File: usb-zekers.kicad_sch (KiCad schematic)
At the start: 0 parts

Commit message: Wire more stuff
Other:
- added sheet Power (power.kicad_sch)
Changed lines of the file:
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@@
+    )
+  )
+  (sheet (at 168.275 111.76) (size 12.7 3.81) (fields_autoplaced)
+    (stroke (width 0.1524) (type solid))
+    (fill (color 0 0 0 0.0000))
+    (property "Sheetname" "Power" (at 168.275 111.0484 0)
+      (effects (font (size 1.27 1.27)) (justify left bottom))
+    )
+    (property "Sheetfile" "power.kicad_sch" (at 168.275 116.1546 0)
+      (effects (font (size 1.27 1.27)) (justify left top))
+    )
+    (instances
+      (project "usb-zekers"
+        (path "/1eef11ed-4055-4fe6-b7fc-0d497914d6cc" (page "6"))
+      )
     )
   )

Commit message: Whole bunch of changes to all kinds of things
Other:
- sheet Connectors ports: added CC_PORT0{CC1, CC2}, SWD{SWDIO,SWDCLK}, VBUS_PORT0, VBUS_PORTA, ~{RESET}; removed none
- sheet MCU ports: added I2C{SDA,SCL}, LED_PORT0{R,G}, NCP0_CLIND, NCP0_EN, NCP0_INT, SWD{SWDIO,SWDCLK}, UCPD1{CC1,CC2}, ~{RESET}; removed none
- sheet Power conversion PORT0 ports: added I2C{SDA,SCL}, NCP0_CLIND, NCP0_EN, NCP0_INT, NCP0_VIN, NCP0_VOUT; removed none
- sheet User Interface ports: added LED_PORT0{R,G}, ~{RESET}; removed none

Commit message: WIP on vconn
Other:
- added sheet VCONN (vconn.kicad_sch)
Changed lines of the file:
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@@
-	(wire
-		(pts
-			(xy 137.16 121.92) (xy 181.61 121.92)
-		)
-		(stroke
-			(width 0)
-			(type default)
-		)
-	)
 	(wire
 		(pts
@@
 		(pts
 			(xy 85.09 93.98) (xy 85.09 106.68)
-		)
-		(stroke
-			(width 0)
-			(type default)
-		)
-	)
-	(wire
-		(pts
-			(xy 181.61 102.87) (xy 181.61 121.92)
 		)
 		(stroke
@@
 				)
 			)
+		)
+	)
+	(sheet
+		(at 161.29 120.65)
+		(size 35.56 24.13)
+		(fields_autoplaced yes)
+		(stroke
+			(width 0.1524)
+			(type solid)
+		)
+		(fill
+			(color 0 0 0 0.0000)
+		)
+		(property "Sheetname" "VCONN"
+			(at 161.29 119.9384 0)
+			(effects
+				(font
+					(size 1.27 1.27)
+				)
+				(justify left bottom)
+			)
+		)
+		(property "Sheetfile" "vconn.kicad_sch"
+			(at 161.29 145.3646 0)
+			(effects
+				(font
+					(size 1.27 1.27)
+				)
+				(justify left top)
+			)
+		)
+		(instances
+			(project "usb-zekers"
+				(path "/1eef11ed-4055-4fe6-b7fc-0d497914d6cc"
+					(page "7")
+				)
+			)

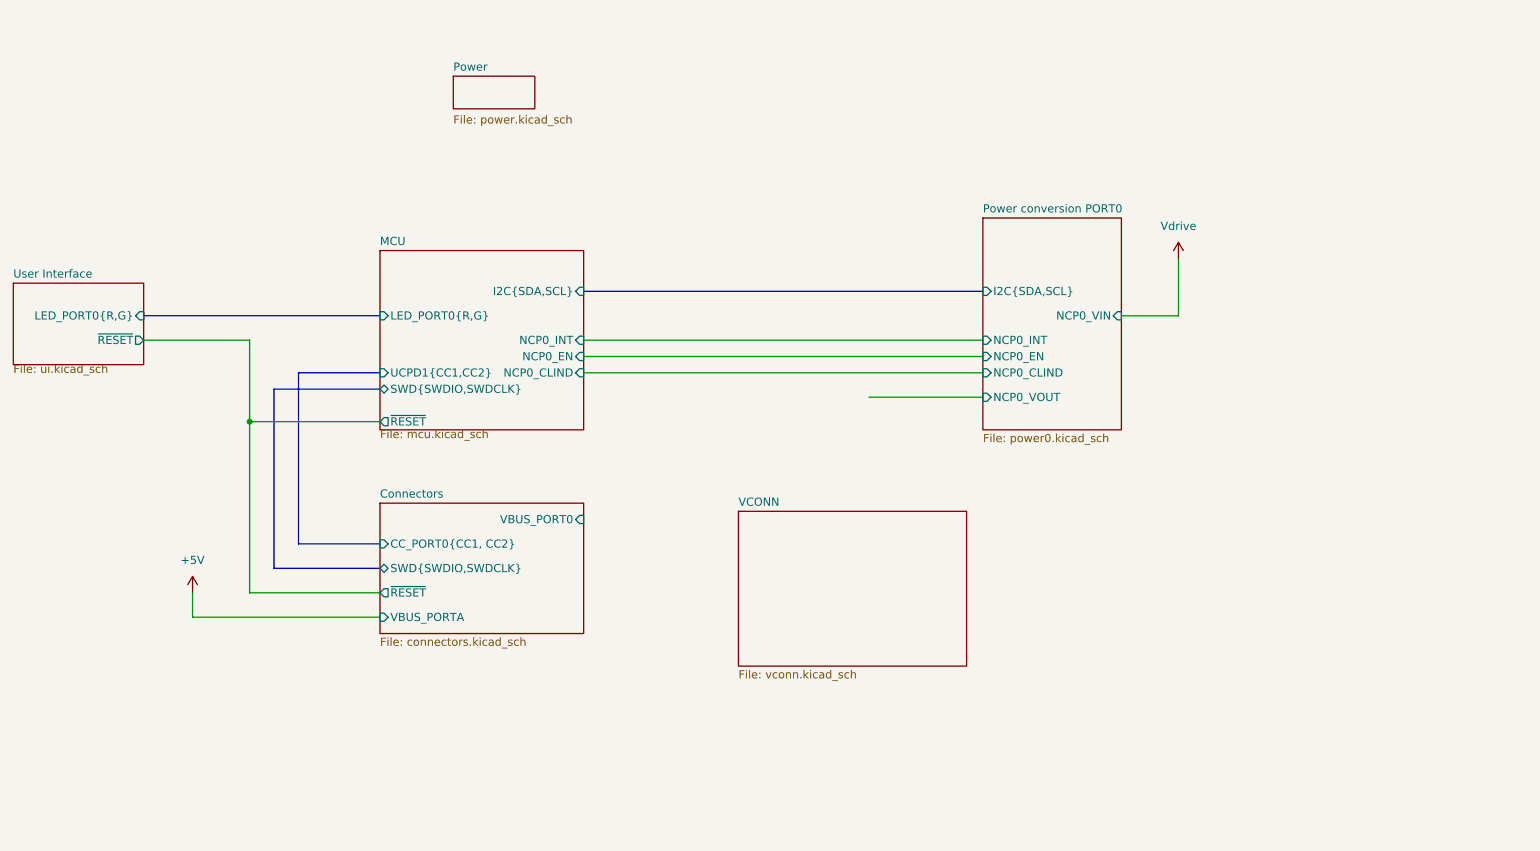
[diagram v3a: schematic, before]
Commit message: wire up vconn stuff
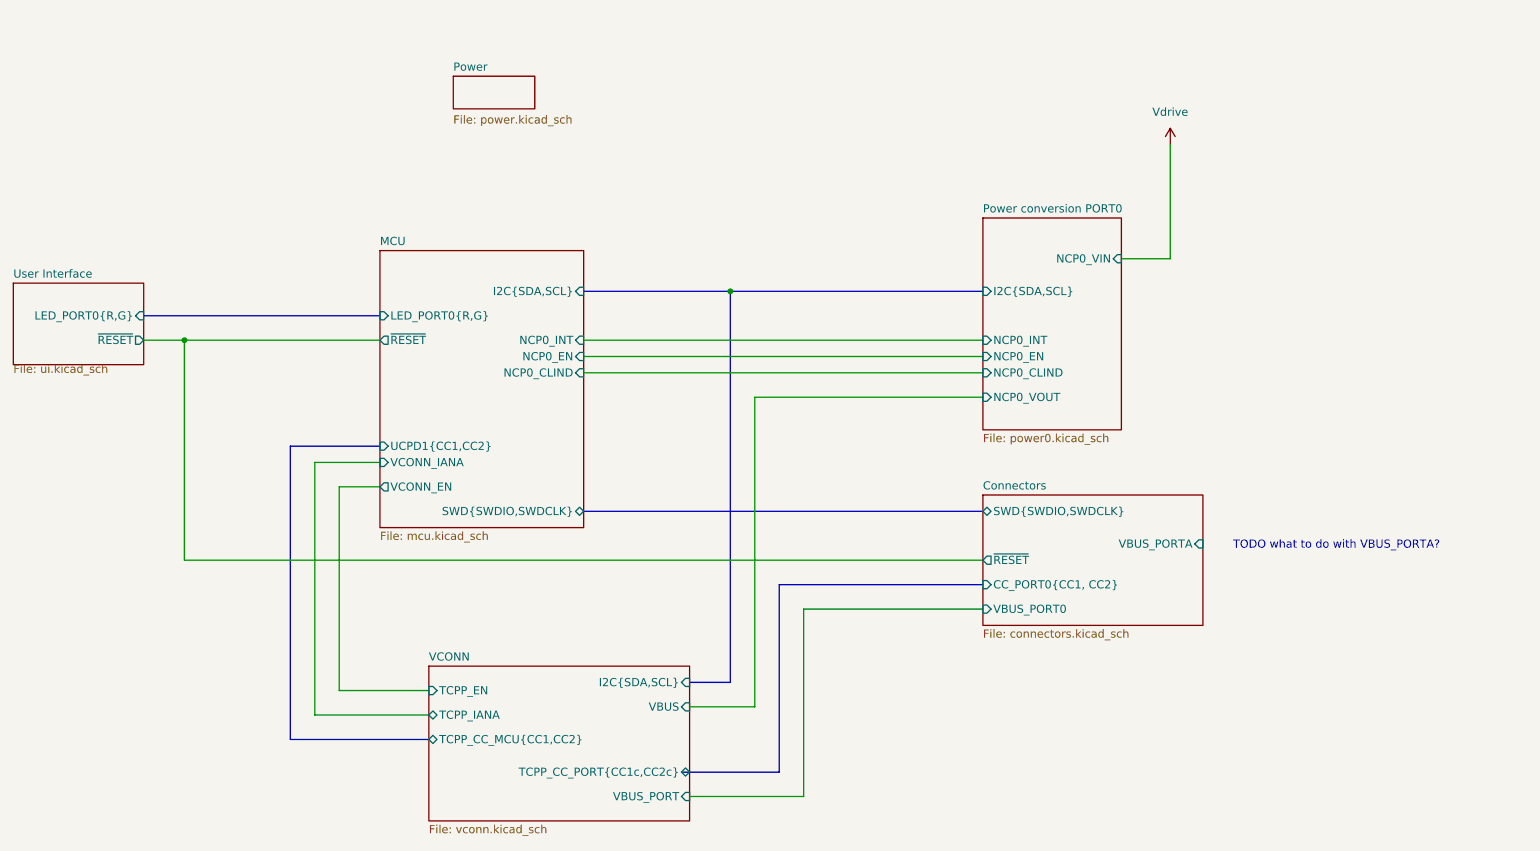
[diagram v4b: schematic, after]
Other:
- sheet MCU ports: added VCONN_EN, VCONN_IANA; removed none
- sheet VCONN ports: added I2C{SDA,SCL}, TCPP_CC_MCU{CC1,CC2}, TCPP_CC_PORT{CC1c,CC2c}, TCPP_EN, TCPP_IANA, VBUS, VBUS_PORT; removed none
- note added: "TODO what to do with VBUS_PORTA?"

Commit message: Wire up vconn and analog pins
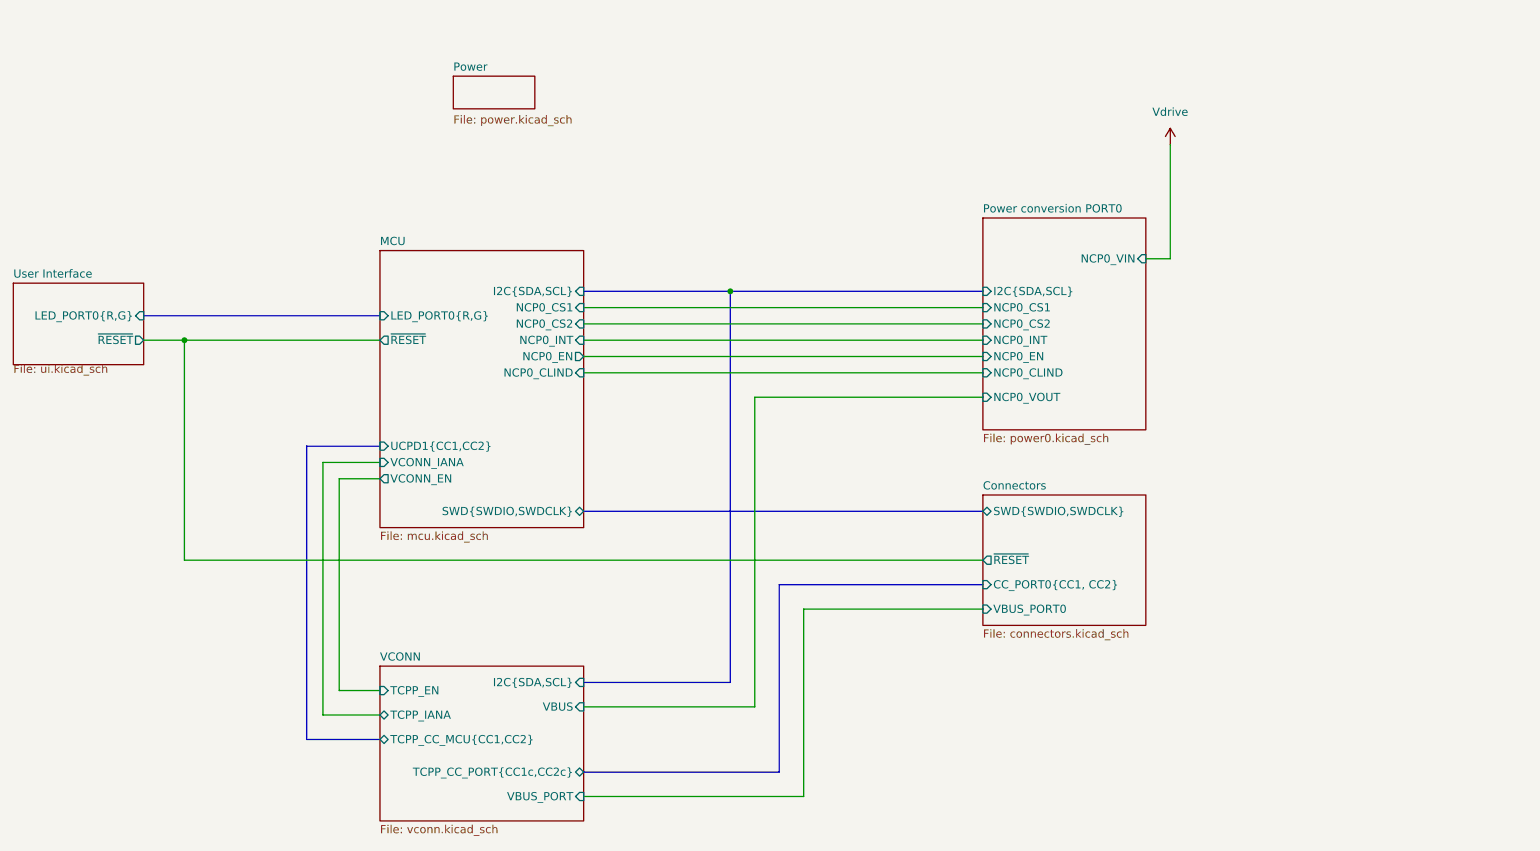
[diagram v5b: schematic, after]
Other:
- sheet Connectors ports: added none; removed VBUS_PORTA
- sheet MCU ports: added NCP0_CS1, NCP0_CS2; removed none
- sheet Power conversion PORT0 ports: added NCP0_CS1, NCP0_CS2; removed none
- note removed: "TODO what to do with VBUS_PORTA?"
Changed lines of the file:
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@@
 		(color 0 0 0 0)
 	)
-	(wire
-		(pts
-			(xy 228.6 81.28) (xy 220.98 81.28)
+	(bus
+		(pts
+			(xy 137.16 147.32) (xy 160.02 147.32)
 		)
 		(stroke
@@
 		)
 	)
-	(bus
-		(pts
-			(xy 153.67 147.32) (xy 160.02 147.32)
+	(wire
+		(pts
+			(xy 137.16 88.9) (xy 199.39 88.9)
 		)
 		(stroke
@@
 		)
 	)
+	(wire
+		(pts
+			(xy 224.79 81.28) (xy 228.6 81.28)
+		)
+		(stroke
+			(width 0)
+			(type default)
+		)
+	)
 	(bus
 		(pts
@@
 	(bus
 		(pts
-			(xy 91.44 110.49) (xy 91.44 156.21)
+			(xy 93.98 110.49) (xy 93.98 156.21)
+		)
+		(stroke
+			(width 0)
+			(type default)
+		)
+	)
+	(wire
+		(pts
+			(xy 137.16 165.1) (xy 171.45 165.1)
 		)
 		(stroke
@@
 	(bus
 		(pts
-			(xy 105.41 110.49) (xy 91.44 110.49)
+			(xy 105.41 110.49) (xy 93.98 110.49)
 		)
 		(stroke
@@
 	(wire
 		(pts
-			(xy 99.06 148.59) (xy 113.03 148.59)
-		)
-		(stroke
-			(width 0)
-			(type default)
-		)
-	)
-	(wire
-		(pts
-			(xy 105.41 116.84) (xy 99.06 116.84)
+			(xy 99.06 148.59) (xy 105.41 148.59)
+		)
+		(stroke
+			(width 0)
+			(type default)
+		)
+	)
+	(wire
+		(pts
+			(xy 105.41 115.57) (xy 99.06 115.57)
 		)
 		(stroke
@@
 	(wire
 		(pts
-			(xy 153.67 151.13) (xy 163.83 151.13)
-		)
-		(stroke
-			(width 0)
-			(type default)
-		)
-	)
-	(wire
-		(pts
-			(xy 153.67 165.1) (xy 171.45 165.1)
-		)
-		(stroke
-			(width 0)
-			(type default)
-		)
-	)
-	(wire
-		(pts
 			(xy 74.93 93.98) (xy 105.41 93.98)
 		)
@@
 	(wire
 		(pts
-			(xy 95.25 113.03) (xy 95.25 152.4)
+			(xy 96.52 113.03) (xy 96.52 152.4)
 		)
 		(stroke
@@
 		)
 	)
+	(bus
+		(pts
+			(xy 137.16 161.29) (xy 167.64 161.29)
+		)
+		(stroke
+			(width 0)
+			(type default)
+		)
+	)
 	(wire
 		(pts
@@
 	(wire
 		(pts
+			(xy 137.16 91.44) (xy 199.39 91.44)
+		)
+		(stroke
+			(width 0)
+			(type default)
+		)
+	)
+	(wire
+		(pts
 			(xy 74.93 128.27) (xy 74.93 93.98)
 		)
@@
 	(bus
 		(pts
-			(xy 91.44 156.21) (xy 113.03 156.21)
+			(xy 93.98 156.21) (xy 105.41 156.21)
+		)
+		(stroke
+			(width 0)
+			(type default)
+		)
+	)
+	(wire
+		(pts
+			(xy 137.16 151.13) (xy 163.83 151.13)
 		)
 		(stroke
@@
 	(wire
 		(pts
-			(xy 99.06 116.84) (xy 99.06 148.59)
+			(xy 99.06 115.57) (xy 99.06 148.59)
 		)
 		(stroke
@@
 	(wire
 		(pts
-			(xy 105.41 113.03) (xy 95.25 113.03)
-		)
-		(stroke
-			(width 0)
-			(type default)
-		)
-	)
-	(wire
-		(pts
-			(xy 95.25 152.4) (xy 113.03 152.4)
-		)
-		(stroke
-			(width 0)
-			(type default)
-		)
-	)
-	(bus
-		(pts
-			(xy 152.4 161.29) (xy 167.64 161.29)
-		)
-		(stroke
-			(width 0)
-			(type default)
-		)
-	)
-	(text "TODO what to do with VBUS_PORTA?\n"
-		(exclude_from_sim no)
-		(at 254.508 125.984 0)
-		(effects
-			(font
-				(size 1.27 1.27)
-			)
+			(xy 105.41 113.03) (xy 96.52 113.03)
+		)
+		(stroke
+			(width 0)
+			(type default)
+		)
+	)
+	(wire
+		(pts
+			(xy 96.52 152.4) (xy 105.41 152.4)
+		)
+		(stroke
+			(width 0)
+			(type default)
 		)
 	)
@@
 	(sheet
 		(at 199.39 118.11)
-		(size 34.29 20.32)
+		(size 25.4 20.32)
 		(fields_autoplaced yes)
 		(stroke
@@
 				)
 				(justify left)
-			)
-		)
-		(pin "VBUS_PORTA" input
-			(at 233.68 125.73 0)
-			(effects
-				(font
-					(size 1.27 1.27)
-				)
-				(justify right)
 			)
 		)
@@
 	)
 	(sheet
-		(at 113.03 144.78)
-		(size 40.64 24.13)
+		(at 105.41 144.78)
+		(size 31.75 24.13)
 		(fields_autoplaced yes)
 		(stroke
@@
 		)
 		(property "Sheetname" "VCONN"
-			(at 113.03 144.0684 0)
+			(at 105.41 144.0684 0)
 			(effects
 				(font
@@
 		)
 		(property "Sheetfile" "vconn.kicad_sch"
-			(at 113.03 169.4946 0)
+			(at 105.41 169.4946 0)
 			(effects
 				(font
@@
 		)
 		(pin "TCPP_EN" input
-			(at 113.03 148.59 180)
+			(at 105.41 148.59 180)
 			(effects
 				(font
@@
 		)
 		(pin "TCPP_CC_MCU{CC1,CC2}" bidirectional
-			(at 113.03 156.21 180)
+			(at 105.41 156.21 180)
 			(effects
 				(font
@@
 		)
 		(pin "TCPP_IANA" bidirectional
-			(at 113.03 152.4 180)
+			(at 105.41 152.4 180)
 			(effects
 				(font
@@
 		)
 		(pin "I2C{SDA,SCL}" input
-			(at 153.67 147.32 0)
+			(at 137.16 147.32 0)
 			(effects
 				(font
@@
 		)
 		(pin "VBUS" input
-			(at 153.67 151.13 0)
+			(at 137.16 151.13 0)
 			(effects
 				(font
@@
 		)
 		(pin "TCPP_CC_PORT{CC1c,CC2c}" bidirectional
-			(at 153.67 161.29 0)
+			(at 137.16 161.29 0)
 			(effects
 				(font
@@
 		)
 		(pin "VBUS_PORT" input
-			(at 153.67 165.1 0)
+			(at 137.16 165.1 0)
 			(effects
 				(font
@@
 			)
 		)
-		(pin "NCP0_EN" input
-			(at 137.16 96.52 0)
-			(effects
-				(font
-					(size 1.27 1.27)
-				)
-				(justify right)
-			)
-		)
 		(pin "NCP0_INT" input
 			(at 137.16 93.98 0)
@@
 		)
 		(pin "VCONN_EN" output
-			(at 105.41 116.84 180)
-			(effects
-				(font
-					(size 1.27 1.27)
-				)
-				(justify left)
+			(at 105.41 115.57 180)
+			(effects
+				(font
+					(size 1.27 1.27)
+				)
+				(justify left)
+			)
+		)
+		(pin "NCP0_CS2" input
+			(at 137.16 91.44 0)
+			(effects
+				(font
+					(size 1.27 1.27)
+				)
+				(justify right)
+			)
+		)
+		(pin "NCP0_CS1" input
+			(at 137.16 88.9 0)
+			(effects
+				(font
+					(size 1.27 1.27)
+				)
+				(justify right)
+			)
+		)
+		(pin "NCP0_EN" output
+			(at 137.16 96.52 0)
+			(effects
+				(font
+					(size 1.27 1.27)
+				)
+				(justify right)
 			)
 		)
@@
 	(sheet
 		(at 199.39 74.93)
-		(size 21.59 33.02)
+		(size 25.4 33.02)
 		(fields_autoplaced yes)
 		(stroke
@@
 		)
 		(pin "NCP0_VIN" input
-			(at 220.98 81.28 0)
+			(at 224.79 81.28 0)
 			(effects
 				(font
@@
 			(effects
 				(font
+					(size 1.27 1.27)
+				)
+				(justify left)
+			)
+		)
+		(pin "NCP0_CS1" input
+			(at 199.39 88.9 180)
+			(effects
+				(font
+					(size 1.27 1.27)
+				)
+				(justify left)
+			)
+		)
+		(pin "NCP0_CS2" input
+			(at 199.39 91.44 180)
+			(effects
+				(font

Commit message: Wire up VCONN_FLGn
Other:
- sheet MCU ports: added VCONN_FLGn; removed none
- sheet VCONN ports: added TCPP_FLGn; removed none
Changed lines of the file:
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@@
 	(wire
 		(pts
-			(xy 171.45 165.1) (xy 171.45 135.89)
+			(xy 171.45 163.83) (xy 171.45 135.89)
 		)
 		(stroke
@@
 	(wire
 		(pts
+			(xy 91.44 157.48) (xy 105.41 157.48)
+		)
+		(stroke
+			(width 0)
+			(type default)
+		)
+	)
+	(wire
+		(pts
+			(xy 105.41 107.95) (xy 91.44 107.95)
+		)
+		(stroke
+			(width 0)
+			(type default)
+		)
+	)
+	(wire
+		(pts
 			(xy 68.58 93.98) (xy 74.93 93.98)
 		)
@@
 	(bus
 		(pts
-			(xy 93.98 110.49) (xy 93.98 156.21)
-		)
-		(stroke
-			(width 0)
-			(type default)
-		)
-	)
-	(wire
-		(pts
-			(xy 137.16 165.1) (xy 171.45 165.1)
+			(xy 93.98 110.49) (xy 93.98 154.94)
+		)
+		(stroke
+			(width 0)
+			(type default)
+		)
+	)
+	(wire
+		(pts
+			(xy 137.16 163.83) (xy 171.45 163.83)
 		)
 		(stroke
@@
 	(wire
 		(pts
-			(xy 99.06 148.59) (xy 105.41 148.59)
+			(xy 99.06 149.86) (xy 105.41 149.86)
 		)
 		(stroke
@@
 	(wire
 		(pts
+			(xy 91.44 107.95) (xy 91.44 157.48)
+		)
+		(stroke
+			(width 0)
+			(type default)
+		)
+	)
+	(wire
+		(pts
 			(xy 74.93 93.98) (xy 105.41 93.98)
 		)
@@
 	(bus
 		(pts
-			(xy 93.98 156.21) (xy 105.41 156.21)
+			(xy 93.98 154.94) (xy 105.41 154.94)
 		)
 		(stroke
@@
 	(wire
 		(pts
-			(xy 99.06 115.57) (xy 99.06 148.59)
+			(xy 99.06 115.57) (xy 99.06 149.86)
 		)
 		(stroke
@@
 		)
 		(pin "TCPP_EN" input
-			(at 105.41 148.59 180)
+			(at 105.41 149.86 180)
 			(effects
 				(font
@@
 		)
 		(pin "TCPP_CC_MCU{CC1,CC2}" bidirectional
-			(at 105.41 156.21 180)
+			(at 105.41 154.94 180)
 			(effects
 				(font
@@
 		)
 		(pin "VBUS_PORT" input
-			(at 137.16 165.1 0)
-			(effects
-				(font
-					(size 1.27 1.27)
-				)
-				(justify right)
+			(at 137.16 163.83 0)
+			(effects
+				(font
+					(size 1.27 1.27)
+				)
+				(justify right)
+			)
+		)
+		(pin "TCPP_FLGn" output
+			(at 105.41 157.48 180)
+			(effects
+				(font
+					(size 1.27 1.27)
+				)
+				(justify left)
 			)
 		)
@@
 			)
 		)
+		(pin "VCONN_FLGn" input
+			(at 105.41 107.95 180)
+			(effects
+				(font
+					(size 1.27 1.27)
+				)
+				(justify left)
+			)
+		)

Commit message: Fix ERC errors, swap out mosfets for NVC chip
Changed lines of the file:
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@@
 	)
 	(sheet
-		(at 116.84 52.832)
-		(size 12.7 5.08)
+		(at 105.41 48.26)
+		(size 31.75 9.652)
 		(fields_autoplaced yes)
 		(stroke
@@
 		)
 		(property "Sheetname" "Power"
-			(at 116.84 52.1204 0)
+			(at 105.41 47.5484 0)
 			(effects
 				(font
@@
 		)
 		(property "Sheetfile" "power.kicad_sch"
-			(at 116.84 58.8776 0)
+			(at 105.41 58.4966 0)
 			(effects
 				(font
